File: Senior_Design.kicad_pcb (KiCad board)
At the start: 2 copper layers, 100 x 100 mm, 158 parts, among them J1001 GS2, J102 GS2, J103 BARREL_JACK, J104 ISP, J1201 USB_A, J1202 USB_A, J1401 USB_OTG, J1402 GS2, J1403 GS2, J1404 GS3, Q1001 MMBT4403, Q101 Q_NMOS_DGS, Q1101 Q_NMOS_DGS, Q1102 Q_PMOS_DGS, Q601 Q_NMOS_DGS, Q602 Q_PMOS_DGS, U1001 HX711, U101 ATMEGA2561-16AU, U1101 MOUDLE-BLUETOOTH-HC-05(34P-27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, U1301 LM358_IC, U1401 FT231XS, U1501 TPS562210, U1701 INA169, U1801 INA169, U1901 INA169, U201 TPS562210, U301 TPS562210, Y101 16MHZ

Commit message: after group meeting
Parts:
- removed C201, C205: 0.1uF, Capacitors_SMD:C_0603
- removed C202, C203: 10uF, Capacitors_SMD:C_0603
- removed C204: 8200pF, Capacitors_SMD:C_0603
- removed C206, C207, C208: 22uF, Capacitors_SMD:C_0603
- removed D201: D_Schottky, sod:SOD-123F
- removed D202: LED, LEDs:LED_0805
- removed R201: 10.0k, Resistors_SMD:R_0603
- removed R202: 100k, Resistors_SMD:R_0603
- removed R203: 33.2k, Resistors_SMD:R_0603
- removed R204: 10k, Resistors_SMD:R_0603
- removed R205: 0.1, Resistors_SMD:R_0603
- removed R206: 1K, Resistors_SMD:R_0603
- removed U201: TPS562210, TO_SOT_Packages_SMD:SOT-23-8
- added D1301: IR204A, LEDs:LED_D5.0mm_Horizontal_O3.81mm_Z3.0mm, F.Cu at (95.5, 146.5)
- added J101: RESET, Buttons_Switches_SMD:SW_SPST_PTS645, F.Cu at (84.5, 116.5)
- added J105: Smraza2004_LCD, Pin_Headers:Pin_Header_Straight_1x04_Pitch2.54mm, F.Cu at (54.0, 104.5)
- added J106: touch(8pos) AT42QT1070 STANDALONE, Pin_Headers:Pin_Header_Straight_2x04_Pitch2.54mm, F.Cu at (54.0, 125.7)
- added L1001: 3.3uH, Inductors_SMD:L_0805, F.Cu at (120.0, 96.9)
- added L1501: 4.7uH, Inductors_SMD:L_Vishay_IHLP-1212, F.Cu at (129.0, 121.3)
- added L301: 4.7uH, Inductors_SMD:L_Vishay_IHLP-1212, F.Cu at (111.8, 72.4)
- added R1403: 10k, Resistors_SMD:R_0603, F.Cu at (84.5, 161.0)
- added R1408: 10k, Resistors_SMD:R_0603, F.Cu at (83.0, 167.5)
- added R1409: 10k, Resistors_SMD:R_0603, F.Cu at (81.5, 163.5)
- added R1410: 1k, Resistors_SMD:R_0603, F.Cu at (77.0, 168.0)
- added R1411: 10k, Resistors_SMD:R_0603, F.Cu at (89.0, 161.5)
- added R1412: 1k, Resistors_SMD:R_0603, F.Cu at (86.0, 173.0)
- added R1413: 10k, Resistors_SMD:R_0603, F.Cu at (89.5, 170.2)
- added R1414: 1k, Resistors_SMD:R_0603, F.Cu at (76.5, 172.5)
- added S1101: button, Buttons_Switches_SMD:SW_SPST_PTS645, F.Cu at (58.5, 92.0)
- added U102: WS2812B, LEDs:LED_WS2812B-PLCC4, F.Cu at (109.5, 54.0)
- added U103: WS2812B_STRIP, Pin_Headers:Pin_Header_Straight_1x03_Pitch2.54mm, F.Cu at (94.0, 53.0)
- D1302: footprint Opto-Devices:PhotoDiode_SFH225 -> LEDs:LED_D1.8mm_W1.8mm_H2.4mm_Horizontal_O3.81mm_Z4.9mm
- J104: footprint connect-thru:2x3-ARRAY_P100mil -> Pin_Headers:Pin_Header_Straight_2x03_Pitch2.54mm
- moved R304 127.1 mm to (102.2, 64.1)
- moved R303 121.2 mm to (102.2, 66.0), turned to 180 degrees
- moved R302 116.0 mm to (110.5, 63.5)
- moved R305 114.5 mm to (108.6, 78.1), turned to 90 degrees
- moved C306 112.6 mm to (106.7, 71.1)
- moved R306 110.3 mm to (111.1, 78.1), turned to 180 degrees
- moved C308 107.0 mm to (106.7, 74.9)
- moved R106 106.5 mm to (87.6, 54.0)
- moved D302 106.1 mm to (109.9, 80.6), turned to 180 degrees
- moved R301 105.8 mm to (102.2, 68.6), turned to 180 degrees
- moved C307 103.8 mm to (106.7, 73.0), turned to 0 degrees
- moved D301 103.3 mm to (106.0, 78.7), turned to 270 degrees
- moved C108 102.9 mm to (82.5, 59.7)
- moved C304 102.6 mm to (106.7, 62.9), turned to 0 degrees
- moved C301 102.0 mm to (115.6, 66.7), turned to 270 degrees
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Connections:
- R105 pad 2: (no net) -> Net-(R105-Pad2)
- R1302 pad 2: (no net) -> Net-(D1301-Pad2)
- U101 pad 25: (no net) -> SCL
- U101 pad 26: (no net) -> SDA
- U101 pad 35: (no net) -> touch_TL
- U101 pad 36: (no net) -> touch_TR
- U101 pad 37: (no net) -> touch_TC
- U101 pad 38: (no net) -> touch_BL
- U101 pad 39: (no net) -> touch_BR
- U101 pad 45: (no net) -> LEDS_Din
- U101 pad 54: (no net) -> 12V_monADC
- U101 pad 55: (no net) -> 5V2_monADC
- U101 pad 56: (no net) -> 5V1_monADC
- U101 pad 57: (no net) -> 3V3_monADC

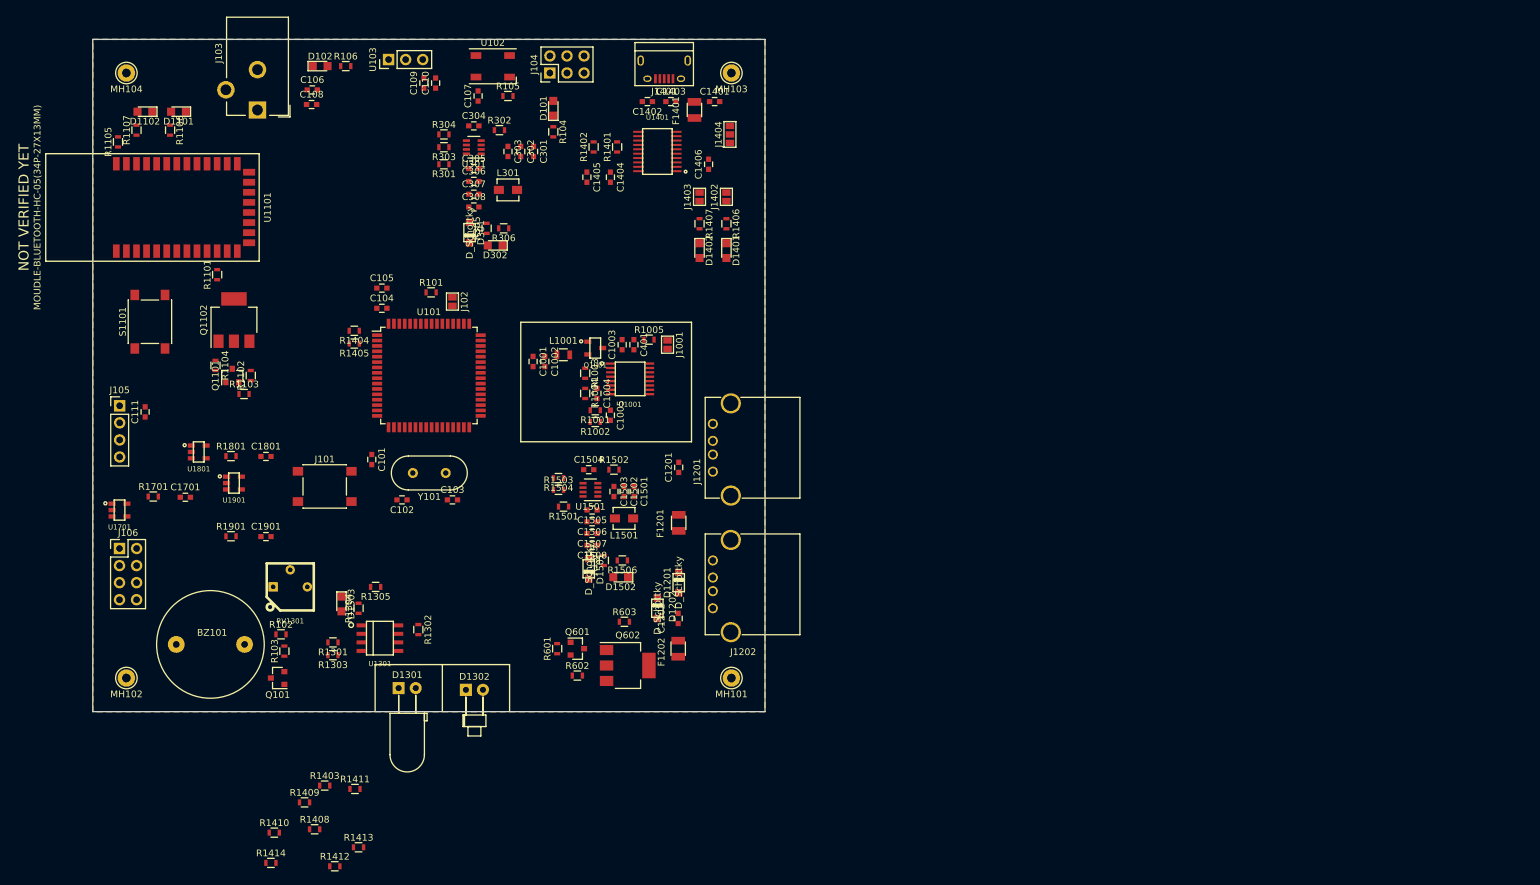
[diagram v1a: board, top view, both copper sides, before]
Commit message: MCU Change ATMEGA328PB
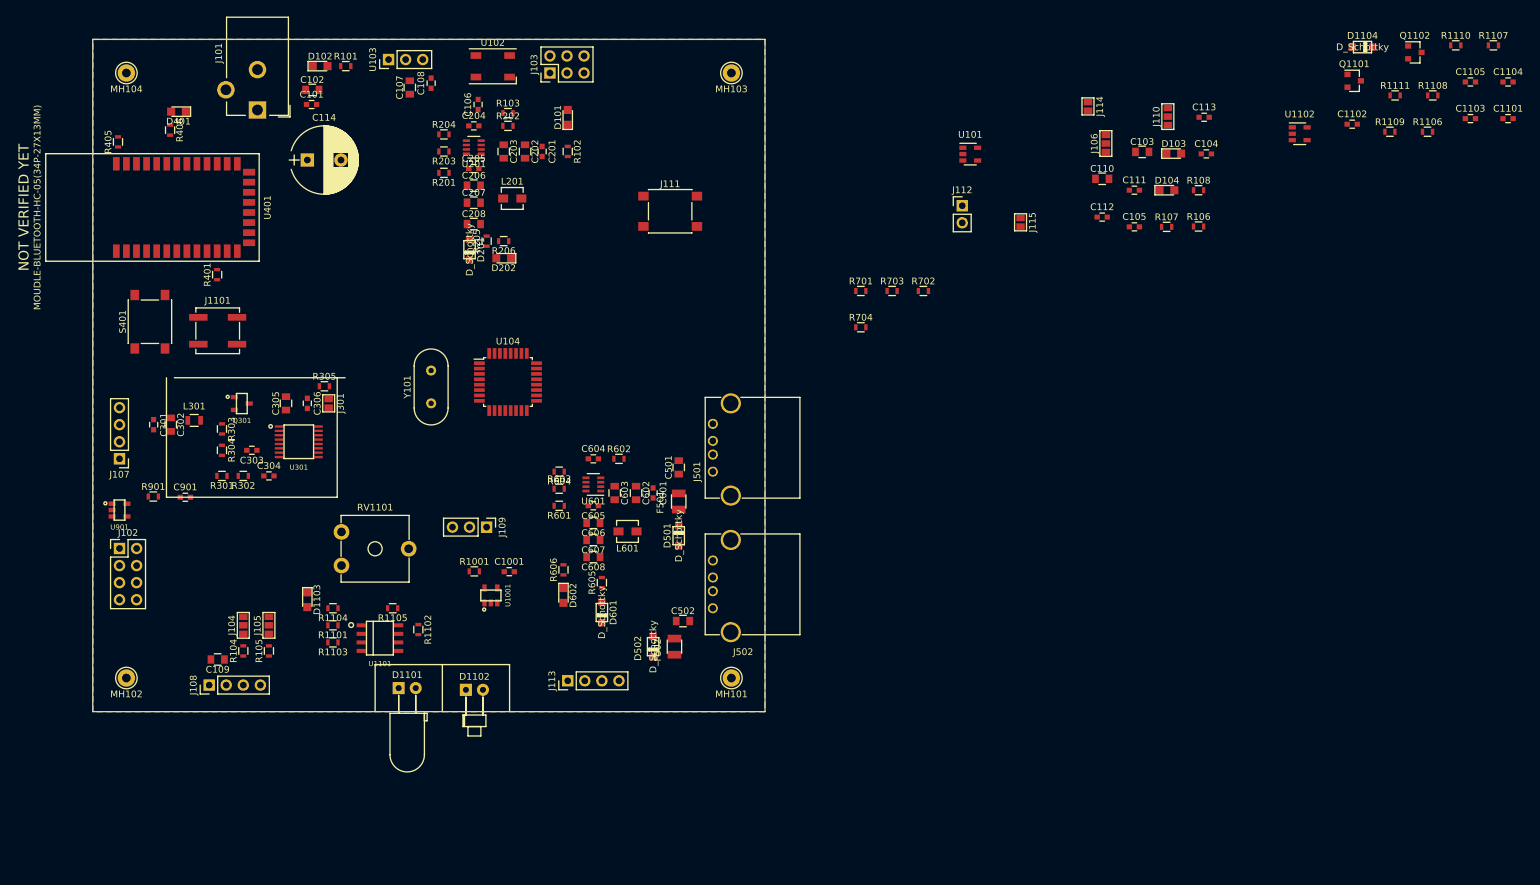
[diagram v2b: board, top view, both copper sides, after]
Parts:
- removed BZ101: Buzzer, Buzzers_Beepers:BUZZER
- removed C1002, C1003, C1201, C1202, C1405, C1502, C1503: 10uF, Capacitors_SMD:C_0603
- removed the C101 at (91.5, 112.5)
- removed the C106 at (82.6, 57.5)
- removed C1401, C1404, C1406, C1901: 0.1uF, Capacitors_SMD:C_0603
- removed C1402, C1403: 47pF, Capacitors_SMD:C_0603
- removed C1506, C1507, C1508, C307, C308: 22uF, Capacitors_SMD:C_0603
- removed the C303 at (111.8, 66.7)
- removed the C306 at (106.7, 71.1)
- removed the D1102 at (57.8, 60.8)
- removed D1401, D1402: LED, LEDs:LED_0805
- removed F1401: Polyfuse, Fuse_Holders_and_Fuses:Fuse_SMD1206_Reflow
- removed the J101 at (84.5, 116.5)
- removed the J102 at (103.5, 89.0)
- removed J1401: USB_OTG, Connectors:USB_Micro-B
- removed J1402, J1403: GS2, Connectors:GS2
- removed J1404: GS3, Connectors:GS3
- removed Q101, Q601: Q_NMOS_DGS, TO_SOT_Packages_SMD:SOT-23
- removed Q602: Q_PMOS_DGS, TO_SOT_Packages_SMD:SOT-223-3_TabPin2
- removed the R101 at (100.3, 87.6)
- removed the R102 at (78.0, 138.5)
- removed the R103 at (78.5, 141.0)
- removed the R1102 at (73.5, 100.0)
- removed the R1103 at (72.5, 102.8)
- removed the R1104 at (68.2, 98.5)
- removed R1401, R1402: 27, Resistors_SMD:R_0603
- removed R1404, R1405, R1406, R1407: 1K, Resistors_SMD:R_0603
- removed R1411, R1413: 10k, Resistors_SMD:R_0603
- removed R1412, R1414: 1k, Resistors_SMD:R_0603
- removed R1901: 10K, Resistors_SMD:R_0603
- removed the R601 at (119.1, 140.6)
- removed the R602 at (122.1, 144.6)
- removed the R603 at (129.1, 136.6)
- removed RV1301: 10K, bourns:BOURNS-3362P_pot
- removed U1401: FT231XS, sop:TSSOP20
- removed U1901: INA169, sot:SOT23-5
- added C107: 10uF, Capacitors_SMD:C_0805, F.Cu at (97.2, 57.1)
- added C110: 10uF, Capacitors_SMD:C_0805, F.Cu at (200.2, 70.7)
- added C1101: 0.1uF, Capacitors_SMD:C_0603, F.Cu at (260.5, 61.8)
- added C1102: 1uF, Capacitors_SMD:C_0603, F.Cu at (237.3, 62.6)
- added C1103: 0.1uF, Capacitors_SMD:C_0603, F.Cu at (254.9, 61.8)
- added C1104: 0.1uF, Capacitors_SMD:C_0603, F.Cu at (260.5, 56.3)
- added C1105: 1uF, Capacitors_SMD:C_0603, F.Cu at (254.9, 56.3)
- added C112: 22pF, Capacitors_SMD:C_0603, F.Cu at (200.2, 76.4)
- added C113: 22pF, Capacitors_SMD:C_0603, F.Cu at (215.3, 61.6)
- added C114: ?uF, Capacitors_THT:CP_Radial_D10.0mm_P5.00mm, F.Cu at (81.9, 67.9)
- added C202: 10uF, Capacitors_SMD:C_0805, F.Cu at (114.3, 66.7)
- added C203: 10uF, Capacitors_SMD:C_0805, F.Cu at (111.1, 66.7)
- added C206: 22uF, Capacitors_SMD:C_0805, F.Cu at (106.7, 71.8)
- added C207: 22uF, Capacitors_SMD:C_0805, F.Cu at (106.7, 74.3)
- added C208: 22uF, Capacitors_SMD:C_0805, F.Cu at (106.7, 77.5)
- added C305: 10uF, Capacitors_SMD:C_0805, F.Cu at (78.7, 104.1)
- added C501: 10uF, Capacitors_SMD:C_0805, F.Cu at (137.2, 113.7)
- added C502: 10uF, Capacitors_SMD:C_0805, F.Cu at (137.8, 136.5)
- added C602: 10uF, Capacitors_SMD:C_0805, F.Cu at (130.8, 117.5)
- added C603: 10uF, Capacitors_SMD:C_0805, F.Cu at (127.6, 117.5)
- added C606: 22uF, Capacitors_SMD:C_0805, F.Cu at (124.5, 121.9)
- added C607: 22uF, Capacitors_SMD:C_0805, F.Cu at (124.5, 124.5)
- added C608: 22uF, Capacitors_SMD:C_0805, F.Cu at (124.5, 127.0)
- added D103: LED, LEDs:LED_0805, F.Cu at (210.8, 67.0)
- added D104: LED, LEDs:LED_0805, F.Cu at (209.8, 72.4)
- added D1104: D_Schottky, sod:SOD-123F, F.Cu at (238.9, 51.1)
- added J103: ISP, Connector_PinHeader_2.54mm:PinHeader_2x03_P2.54mm_Vertical, F.Cu at (118.0, 55.0)
- added J105: GS3, Connectors:GS3, F.Cu at (76.2, 137.2)
- added J106: GS3, Connectors:GS3, F.Cu at (200.7, 65.5)
- added J107: LoadCell_Conn, Connector_PinHeader_2.54mm:PinHeader_1x04_P2.54mm_Vertical, F.Cu at (54.0, 112.4)
- added J109: ambientLight, Connector_PinHeader_2.54mm:PinHeader_1x03_P2.54mm_Vertical, F.Cu at (108.6, 122.6)
- added J110: GS3, Connectors:GS3, F.Cu at (209.9, 61.5)
- added J1101: BLE_RESET, Buttons_Switches_SMD:SW_SPST_B3SL-1002P, F.Cu at (68.6, 93.3)
- added J111: RESET, Buttons_Switches_SMD:SW_SPST_PTS645, F.Cu at (135.9, 75.6)
- added J112: Serial Monitor, Connector_PinHeader_2.54mm:PinHeader_1x02_P2.54mm_Vertical, F.Cu at (179.3, 74.7)
- added J113: breakout, Connector_PinHeader_2.54mm:PinHeader_1x04_P2.54mm_Vertical, F.Cu at (120.7, 145.4)
- added J114: GS2, Connectors:GS2, F.Cu at (198.0, 60.0)
- added J115: GS2, Connectors:GS2, F.Cu at (188.0, 77.2)
- added R104: 100K, Resistors_SMD:R_0603, F.Cu at (72.4, 141.0)
- added R105: 100K, Resistors_SMD:R_0603, F.Cu at (76.2, 141.0)
- added R106: 10k, Resistors_SMD:R_0603, F.Cu at (214.5, 77.8)
- added R107: 500, Resistors_SMD:R_0603, F.Cu at (209.7, 77.9)
- added R108: 500, Resistors_SMD:R_0603, F.Cu at (214.5, 72.4)
- added R1106: 10K, Resistors_SMD:R_0603, F.Cu at (248.5, 63.7)
- added R1108: 10K, Resistors_SMD:R_0603, F.Cu at (249.3, 58.3)
- added R1109: 10K, Resistors_SMD:R_0603, F.Cu at (242.9, 63.7)
- added R1110: 10K, Resistors_SMD:R_0603, F.Cu at (252.7, 50.9)
- added R1111: 10K, Resistors_SMD:R_0603, F.Cu at (243.7, 58.3)
- added RV1101: 10K, Potentiometers:Potentiometer_Trimmer_ACP_CA9v_Horizontal_Px10.0mm_Py5.0mm, F.Cu at (87.0, 128.3)
- added U104: ATMEGA328PB-AU, Housings_QFP:TQFP-32_7x7mm_Pitch0.8mm, F.Cu at (111.8, 101.0)
- added U1102: LP2985-3.3, TO_SOT_Packages_SMD:SOT-23-5, F.Cu at (229.5, 64.0)
- C102, C103: value 22pF -> 10uF; footprint Capacitors_SMD:C_0603 -> Capacitors_SMD:C_0805
- C104, C111: value 10uF -> 0.1uF
- C109, C302: footprint Capacitors_SMD:C_0603 -> Capacitors_SMD:C_0805
- J104: value ISP -> GS3; footprint Pin_Headers:Pin_Header_Straight_2x03_Pitch2.54mm -> Connectors:GS3
- Q1101: value Q_NMOS_DGS -> BSS138
- Q1102: value Q_PMOS_DGS -> BSS138; footprint TO_SOT_Packages_SMD:SOT-223-3_TabPin2 -> TO_SOT_Packages_SMD:SOT-23
- R1107: value 2K -> 100K
- R405: renamed from R1105; value 2K -> 10K
- R704: renamed from R1410; value 1k -> 10k
- U101: value ATMEGA2561-16AU -> MIC5504-3.3YM5; footprint Housings_QFP:TQFP-64_14x14mm_Pitch0.8mm -> TO_SOT_Packages_SMD:SOT-23-5
- moved R1107 202.2 mm to (258.3, 50.9), turned to 0 degrees
- moved Q1102 180.1 mm to (246.7, 51.9), turned to 0 degrees
- moved Q1101 172.6 mm to (237.6, 56.2), turned to 0 degrees
- moved C111 150.8 mm to (204.9, 72.4), turned to 0 degrees
- moved C104 124.8 mm to (215.6, 67.0)
- moved R702 120.9 mm to (173.6, 87.4)
- moved R703 115.9 mm to (168.9, 87.4)
- moved R704 115.2 mm to (164.3, 92.8)
- moved C103 114.9 mm to (206.1, 66.7)
- moved C105 112.3 mm to (204.9, 77.9)
- moved R701 108.5 mm to (164.3, 87.4)
- moved J104 94.0 mm to (72.4, 137.2), turned to 0 degrees
- moved C109 91.1 mm to (68.6, 142.2), turned to 180 degrees
- moved U101 87.0 mm to (180.5, 67.1)
- moved C302 66.1 mm to (61.6, 107.3)
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- renumbered C1801 to C1001, C108 to C101, C107 to C106, C110 to C108, C301 to C201, C304 to C204, C305 to C205, C1001 to C301, C1004 to C303, C1005 to C304, C401 to C306, C1501 to C601, C1504 to C604, C1505 to C605, C1701 to C901, D1301 to D1101, D1302 to D1102, D1303 to D1103, D301 to D201, D302 to D202, D1101 to D401, D1201 to D501, D1202 to D502, D1501 to D601, D1502 to D602, F1201 to F501, F1202 to F502, J103 to J101, J106 to J102, J105 to J108, J1001 to J301, J1201 to J501, J1202 to J502, L301 to L201, L1001 to L301, L1501 to L601, Q1001 to Q301, R1801 to R1001, R106 to R101, R104 to R102, R105 to R103, R1301 to R1101, R1302 to R1102, R1303 to R1103, R1304 to R1104, R1305 to R1105, R301 to R201, R302 to R202, R303 to R203, R304 to R204, R305 to R205, R306 to R206, R1001 to R301, R1002 to R302, R1003 to R303, R1004 to R304, R1005 to R305, R1101 to R401, R1106 to R406, R1501 to R601, R1502 to R602, R1503 to R603, R1504 to R604, R1505 to R605, R1506 to R606, R1403 to R701, R1408 to R702, R1409 to R703, R1701 to R901, S1101 to S401, U1801 to U1001, U1301 to U1101, U301 to U201, U1001 to U301, U1101 to U401, U1501 to U601, U1701 to U901
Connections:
- C1001 pad 1: 3V3-BUS -> 5V-BUS
- C102 pad 1: Net-(C102-Pad1) -> +12V
- C103 pad 1: Net-(C103-Pad1) -> +12V
- C104 pad 2: MCU_VCC_5V -> 5V-BUS
- C105 pad 2: MCU_VCC_5V -> 3V3-BUS
- C109 pad 1: GND -> 5V-BUS
- C109 pad 2: 5V-BUS -> GND
- C111 pad 1: 5V-BUS -> GND
- C111 pad 2: GND -> 5V-BUS
- C302 pad 1: +12V -> SCALE_E+
- C901 pad 1: 3V3-BUS -> 5V-BUS
- D1102 pad 1: 3V3-BUS -> 5V-BUS
- D501 pad 2: 5V-BUS -> /USB/5V
- D502 pad 2: 5V-BUS -> /USB/5V
- J101 pad 2: (no net) -> GND
- J102 pad 1: (no net) -> touch_1
- J102 pad 2: 3V3-BUS -> 5V-BUS
- J102 pad 3: touch_TL -> touch_2
- J102 pad 5: touch_TR -> touch_3
- J102 pad 6: touch_BR -> (no net)
- J102 pad 7: touch_TC -> touch_4
- J102 pad 8: touch_BL -> touch_5
- J104 pad 1: MISO -> GND
- J104 pad 2: MCU_VCC_5V -> Net-(J104-Pad2)
- J104 pad 3: SCK -> 5V-BUS
- Q1101 pad 1: Net-(Q1101-Pad1) -> /Bluetooth/3_3V
- Q1101 pad 2: Net-(Q1101-Pad2) -> /Bluetooth/RX_3v3
- Q1101 pad 3: GND -> B_TX
- Q1102 pad 1: 3V3-BUS -> /Bluetooth/3_3V
- Q1102 pad 2: Net-(Q1101-Pad1) -> /Bluetooth/TX_3v3
- Q1102 pad 3: /Bluetooth/3_3V -> B_RX
- R1001 pad 2: 5V_curMon_ADC -> 5V_curMon_USBLINE_ADC
- R1101 pad 2: Motion_Signal1 -> (no net)
- R1102 pad 1: 3V3-BUS -> 5V-BUS
- R1105 pad 1: 3V3-BUS -> 5V-BUS
- R1107 pad 2: BT_STATE -> Net-(R1106-Pad1)
- R201 pad 2: 5v_En -> +12V
- R202 pad 1: 5V1_PG -> /5V-Regulator/PG
- R301 pad 2: (no net) -> SCALE_A-
- R302 pad 2: (no net) -> SCALE_A+
- R405 pad 1: BT_KEY -> GND
- R601 pad 2: 5v_En_USBLINE -> +12V
- R602 pad 1: 5V2_PG -> /5V-Regulator/PG
- R701 pad 1: 3V3-BUS -> 5V-BUS
- R701 pad 2: 3V3_monADC -> 5V1_monADC
- R702 pad 1: 3V3_monADC -> 5V1_monADC
- R703 pad 1: 5V-BUS -> 5V-BUS_USBLINE
- R703 pad 2: 5V1_monADC -> 5V2_monADC
- R704 pad 1: 5V1_monADC -> 5V2_monADC
- R901 pad 2: 3_3V_curMon_ADC -> 5V_curMon_ADC
- U1001 pad 1: 5V_curMon_ADC -> 5V_curMon_USBLINE_ADC
- U1001 pad 3: 5V_curMon+ -> 5V_curMon+_USBLINE
- U1001 pad 4: 5V_curMon- -> 5V_curMon-_USBLINE
- U1001 pad 5: 3V3-BUS -> 5V-BUS
- U101 pad 1: Motion_Signal1 -> 5V-BUS
- U101 pad 2: MCU_RX1 -> GND
- U101 pad 3: MCU_TX1 -> (no net)
- U102 pad 2: (no net) -> LEDS_Din
- U1101 pad 8: 3V3-BUS -> 5V-BUS
- U201 pad 4: 5V1_PG -> /5V-Regulator/PG
- U401 pad 1: MCU_RX2 -> B_RX
- U401 pad 2: MCU_TX2 -> B_TX
- U601 pad 4: 5V2_PG -> /5V-Regulator/PG
- U901 pad 1: 3_3V_curMon_ADC -> 5V_curMon_ADC
- U901 pad 3: 3_3V_curMon+ -> 5V_curMon+
- U901 pad 4: 3_3V_curMon- -> 5V_curMon-
- U901 pad 5: 3V3-BUS -> 5V-BUS
- Y101 pad 1: Net-(C103-Pad1) -> Net-(C113-Pad1)
- Y101 pad 2: Net-(C102-Pad1) -> Net-(C112-Pad1)

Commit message: all components on board, needs routing
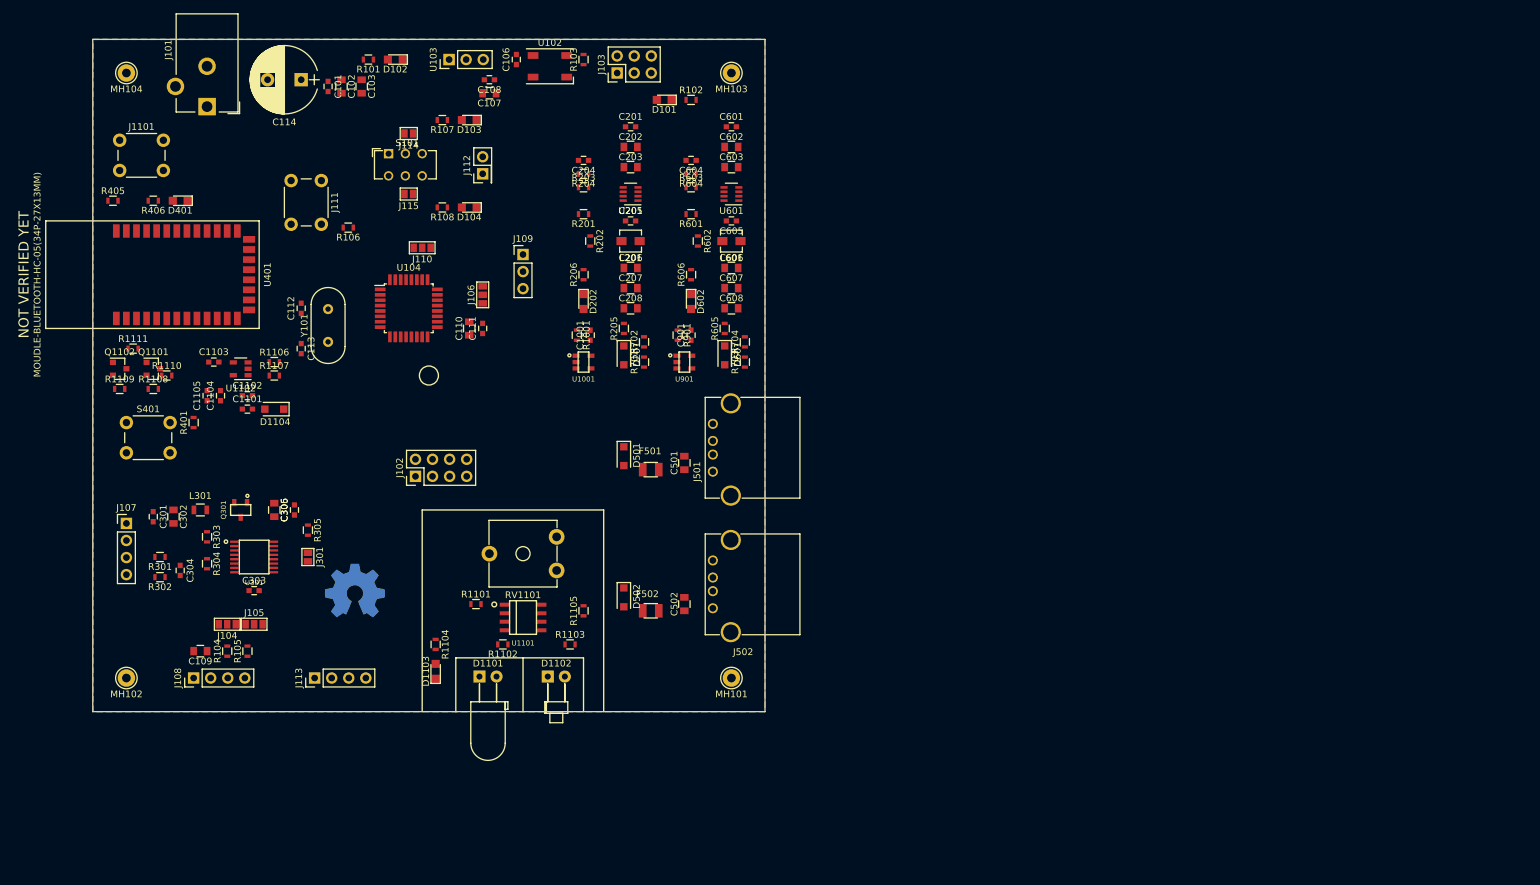
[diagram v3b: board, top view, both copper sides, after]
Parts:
- removed C104, C105: 0.1uF, Capacitors_SMD:C_0603
- removed U101: MIC5504-3.3YM5, TO_SOT_Packages_SMD:SOT-23-5
- added REF***: KiCad-Logo2_12mm_SilkScreen, Symbols:KiCad-Logo2_12mm_SilkScreen, B.Cu at (125.0, 134.0)
- added REF***: OSHW-Symbol_8.9x8mm_Copper, Symbols:OSHW-Symbol_8.9x8mm_Copper, B.Cu at (89.0, 132.0)
- added S101: Serial Switch, Buttons_Switches_THT:SW_CuK_JS202011CQN_DPDT_Straight, F.Cu at (94.0, 67.0)
- D1104, D201, D501, D502, D601: footprint sod:SOD-123F -> Diodes_SMD:D_SOD-123F
- J103: footprint Connector_PinHeader_2.54mm:PinHeader_2x03_P2.54mm_Vertical -> Pin_Headers:Pin_Header_Straight_2x03_Pitch2.54mm
- J107, J113: footprint Connector_PinHeader_2.54mm:PinHeader_1x04_P2.54mm_Vertical -> Pin_Headers:Pin_Header_Straight_1x04_Pitch2.54mm
- J109: footprint Connector_PinHeader_2.54mm:PinHeader_1x03_P2.54mm_Vertical -> Pin_Headers:Pin_Header_Straight_1x03_Pitch2.54mm
- J1101: footprint Buttons_Switches_SMD:SW_SPST_B3SL-1002P -> Buttons_Switches_THT:SW_PUSH_6mm
- J111, S401: footprint Buttons_Switches_SMD:SW_SPST_PTS645 -> Buttons_Switches_THT:SW_PUSH_6mm
- J112: footprint Connector_PinHeader_2.54mm:PinHeader_1x02_P2.54mm_Vertical -> Pin_Headers:Pin_Header_Straight_2x01_Pitch2.54mm
- moved Q1102 198.3 mm to (54.0, 99.0)
- moved R1110 197.9 mm to (61.0, 100.0)
- moved C1104 197.1 mm to (69.0, 103.0), turned to 90 degrees
- moved R1108 195.3 mm to (59.0, 102.0)
- moved C1105 193.6 mm to (67.0, 103.0), turned to 90 degrees
- moved R1109 192.8 mm to (54.0, 102.0)
- moved C1101 192.4 mm to (73.0, 105.0)
- moved R1111 191.5 mm to (56.0, 96.0)
- moved C1103 190.4 mm to (68.0, 98.0)
- moved R1107 187.9 mm to (77.0, 100.0)
- moved Q1101 183.7 mm to (59.0, 99.0)
- moved R1106 174.9 mm to (77.0, 98.0)
- moved D1104 170.6 mm to (77.0, 105.0), turned to 180 degrees
- moved C1102 169.2 mm to (73.0, 103.0)
- moved U1102 161.4 mm to (72.0, 99.0), turned to 180 degrees
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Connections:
- J106 pad 3: breakout_1A -> breakout_2A
- J112 pad 1: (no net) -> /TX
- J112 pad 2: (no net) -> /RX
- J113 pad 2: (no net) -> breakout_2A
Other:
- board text added: "Senior Design Smart Table PCB Designed by Theodore Cox"

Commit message: before meeting
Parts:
- removed REF***: KiCad-Logo2_12mm_SilkScreen, Symbols:KiCad-Logo2_12mm_SilkScreen
- removed REF***: OSHW-Symbol_8.9x8mm_Copper, Symbols:OSHW-Symbol_8.9x8mm_Copper
- moved D103 13.0 mm to (93.0, 62.0), turned to 0 degrees
- moved R107 5.00 mm to (97.0, 62.0), turned to 0 degrees
- moved R1110 4.00 mm to (61.0, 96.0)
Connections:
- J102 pad 1: touch_1 -> 5V-BUS
- J102 pad 2: 5V-BUS -> touch_4
- J102 pad 3: touch_2 -> GND
- J102 pad 4: GND -> touch_5
- J102 pad 5: touch_3 -> GND
- J102 pad 6: (no net) -> touch_1
- J102 pad 7: touch_4 -> touch_3
- J102 pad 8: touch_5 -> touch_2
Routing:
- net +12V: track 0.00 -> 99.3 mm
- net touch_4: track 0.00 -> 29.9 mm
- net touch_5: track 0.00 -> 28.6 mm
- net touch_3: track 0.00 -> 25.4 mm
- net touch_2: track 0.00 -> 21.6 mm
- net touch_1: track 0.00 -> 20.9 mm
- net Net-(R401-Pad2): track 0.00 -> 20.0 mm
- net /5V-Regulator/PG: track 0.00 -> 16.8 mm, vias 0 -> 2
- net 5V_curMon+: track 0.00 -> 15.1 mm
- net B_TX: track 0.00 -> 11.3 mm
- net Net-(C205-Pad2): track 0.00 -> 10.5 mm
- net B_RX: track 0.00 -> 8.33 mm
- net Net-(C204-Pad1): track 0.00 -> 6.82 mm
- net Net-(R201-Pad1): track 0.00 -> 6.37 mm
- net Net-(C205-Pad1): track 0.00 -> 3.11 mm
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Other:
- board text removed: "Senior Design Smart Table PCB Designed by Theodore Cox"
